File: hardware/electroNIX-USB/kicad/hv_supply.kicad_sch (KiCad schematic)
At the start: 25 parts, among them Q3 IRLR3110ZPBF

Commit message: electroNIX-USB: boost gate pull-down gate-to-source as on PCB-036
R45 on PCB-036 pulls the FET gate (after the 10R) to GND; ours sat on
the IO2 side. Move it to the gate and place it at the gate pad. Add a
note listing what was checked against the PCB-036 schematic.

Co-Authored-By: Claude Opus 5.5 <noreply@anthropic.com>
Claude-Session: https://claude.ai/code/session_01AFMfevKEKDGbci8uJGhf4W
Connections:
- net PWM: no longer R9.1
- net at Q3.1 (G), R8.2: now also R9.1
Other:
- note added: "IO2 drives the logic-level FET directly, 32 kHz, duty clamped to ~41 % by firmware (HV_DUTY_MAX). 10k gate-source keeps the FET off (and IO2 low) during boot."
- note removed: "IO2 drives the logic-level FET directly, 32 kHz, duty clamped to ~41 % by firmware (HV_DUTY_MAX). 10k keeps the gate (and IO2) low during boot."
- moved on the sheet: R9
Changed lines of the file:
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@@
   (wire
     (pts
-      (xy 85.09 91.44)
-      (xy 85.09 88.9))
-    (stroke
-      (width 0)
-      (type default))
-)
-  (wire
-    (pts
-      (xy 85.09 99.06)
-      (xy 85.09 101.6))
-    (stroke
-      (width 0)
-      (type default))
+      (xy 95.25 87.63)
+      (xy 95.25 90.17))
+    (stroke
+      (width 0)
+      (type default))
+)
+  (junction
+    (at 94.92 80.01)
+    (diameter 0)
+    (color 0 0 0 0)
 )
   (wire
@@
     (property "Intersheetrefs" "${INTERSHEET_REFS}"
       (at 85.09 80.01 0)
-      (effects
-        (font
-          (size 1.27 1.27)) hide)))
-  (global_label "PWM"
-    (shape passive)
-    (at 85.09 88.9 90)
-    (fields_autoplaced)
-    (effects
-      (font
-        (size 1.27 1.27))
-      (justify left))
-    (property "Intersheetrefs" "${INTERSHEET_REFS}"
-      (at 85.09 88.9 0)
       (effects
         (font
@@
       (justify left top))
 )
-  (text "IO2 drives the logic-level FET directly, 32 kHz,\nduty clamped to ~41 % by firmware (HV_DUTY_MAX).\n10k keeps the gate (and IO2) low during boot."
+  (text "IO2 drives the logic-level FET directly, 32 kHz,\nduty clamped to ~41 % by firmware (HV_DUTY_MAX).\n10k gate-source keeps the FET off (and IO2 low) during boot."
     (at 25 105 0)
     (effects
@@
   (symbol
     (lib_id "power:GND")
-    (at 85.09 101.6 0)
+    (at 95.25 90.17 0)
     (unit 1)
     (in_bom yes)
@@
     (dnp no)
     (property "Reference" "#PWR4011"
-      (at 85.09 101.6 0)
+      (at 95.25 90.17 0)
       (effects
         (font
           (size 1.27 1.27)) hide))
     (property "Value" "GND"
-      (at 85.09 104.8 0)
+      (at 95.25 93.37 0)
       (effects
         (font
           (size 1.27 1.27))))
     (property "Footprint" ""
-      (at 85.09 101.6 0)
+      (at 95.25 90.17 0)
       (effects
         (font
           (size 1.27 1.27)) hide))
     (property "Datasheet" ""
-      (at 85.09 101.6 0)
+      (at 95.25 90.17 0)
       (effects
         (font
@@
   (symbol
     (lib_id "Device:R")
-    (at 85.09 95.25 0)
+    (at 95.25 83.82 0)
     (unit 1)
     (in_bom yes)
@@
     (dnp no)
     (property "Reference" "R9"
-      (at 86.36 93.98 0)
+      (at 96.52 82.55 0)
       (effects
         (font
@@
         (justify left)))
     (property "Value" "10k"
-      (at 86.36 96.52 0)
+      (at 96.52 85.09 0)
       (effects
         (font
@@
         (justify left)))
     (property "Footprint" "Resistor_SMD:R_0805_2012Metric"
-      (at 85.09 95.25 0)
+      (at 95.25 83.82 0)
       (effects
         (font
@@
         (justify left) hide))
     (property "Datasheet" "~"
-      (at 85.09 95.25 0)
-      (effects
-        (font
+      (at 95.25 83.82 0)
+      (effects
+        (font

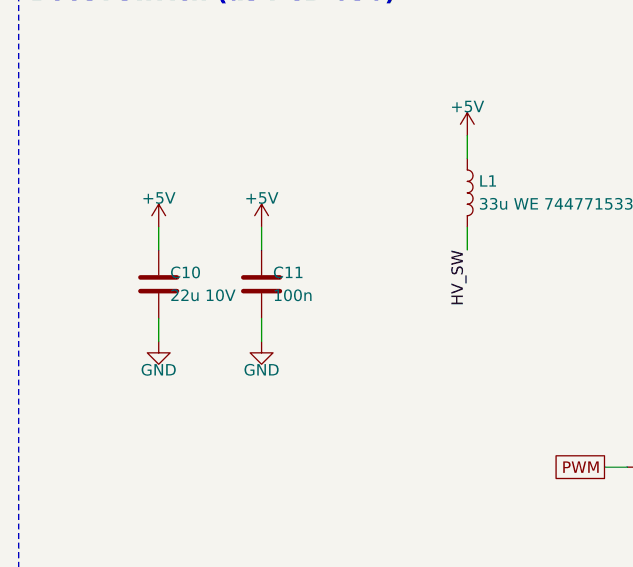
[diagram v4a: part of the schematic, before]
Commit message: electroNIX-USB: tantalum bulk caps on the 5 V input and boost input
Back to PCB-036's 22 uF/35 V tantalum (7343 D case) for the boost input
and use the same part for the USB-C bulk cap. It holds its value at 5 V,
unlike a small MLCC, and its ESR damps hot-plug ringing on the cable.
The 100 nF ceramics stay. Placement adjusted around the larger parts.

Co-Authored-By: Claude Opus 5.5 <noreply@anthropic.com>
Claude-Session: https://claude.ai/code/session_01AFMfevKEKDGbci8uJGhf4W
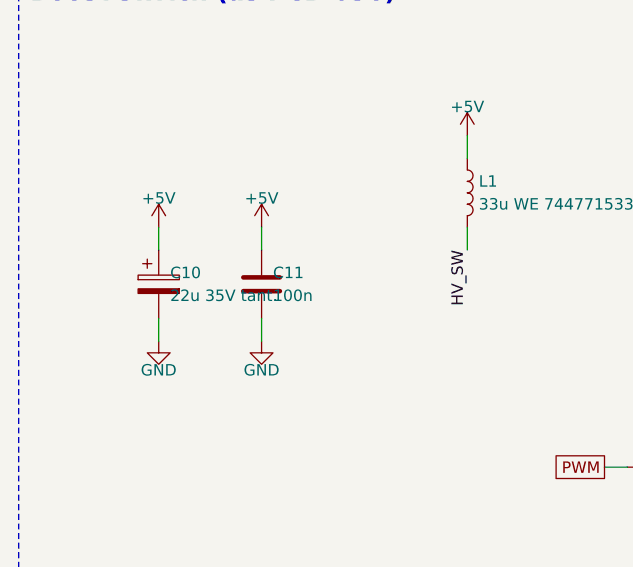
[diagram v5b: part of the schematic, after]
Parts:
- C10: value 22u 10V -> 22u 35V tant.; footprint Capacitor_SMD:C_1206_3216Metric -> Capacitor_Tantalum_SMD:CP_EIA-7343-31_Kemet-D; symbol Device:C -> Device:C_Polarized
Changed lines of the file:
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@@
           (unit 1)))))
   (symbol
-    (lib_id "Device:C")
+    (lib_id "Device:C_Polarized")
     (at 35.56 59.69 0)
     (unit 1)
@@
           (size 1.27 1.27))
         (justify left)))
-    (property "Value" "22u 10V"
+    (property "Value" "22u 35V tant."
       (at 36.83 60.96 0)
       (effects
@@
           (size 1.27 1.27))
         (justify left)))
-    (property "Footprint" "Capacitor_SMD:C_1206_3216Metric"
+    (property "Footprint" "Capacitor_Tantalum_SMD:CP_EIA-7343-31_Kemet-D"
       (at 35.56 59.69 0)
       (effects

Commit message: electroNIX-USB: lay the 170 V output electrolytic flat
New footprint CP_Radial_D8mm_P2.50mm_Lying (2.5 mm leads, keep-clear for
a body up to 8 x 12.5 mm folded flat). C19 now runs along the left edge
toward the front; KBIAS parts and the cathode row moved right to clear it.

Co-Authored-By: Claude Opus 5.5 <noreply@anthropic.com>
Claude-Session: https://claude.ai/code/session_01AFMfevKEKDGbci8uJGhf4W
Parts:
- C19: footprint Capacitor_THT:CP_Radial_D6.3mm_P2.50mm -> electronix:CP_Radial_D8mm_P2.50mm_Lying
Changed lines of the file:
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@@
           (size 1.27 1.27))
         (justify left)))
-    (property "Footprint" "Capacitor_THT:CP_Radial_D6.3mm_P2.50mm"
+    (property "Footprint" "electronix:CP_Radial_D8mm_P2.50mm_Lying"
       (at 44.45 165.1 0)
       (effects
